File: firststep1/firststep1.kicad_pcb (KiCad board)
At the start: 2 copper layers, 30.5 x 22.9 mm, 12 parts, among them J1 Conn_01x02, J2 Conn_01x03_Male, U1 LM317_TO-220, U2 TL431LP

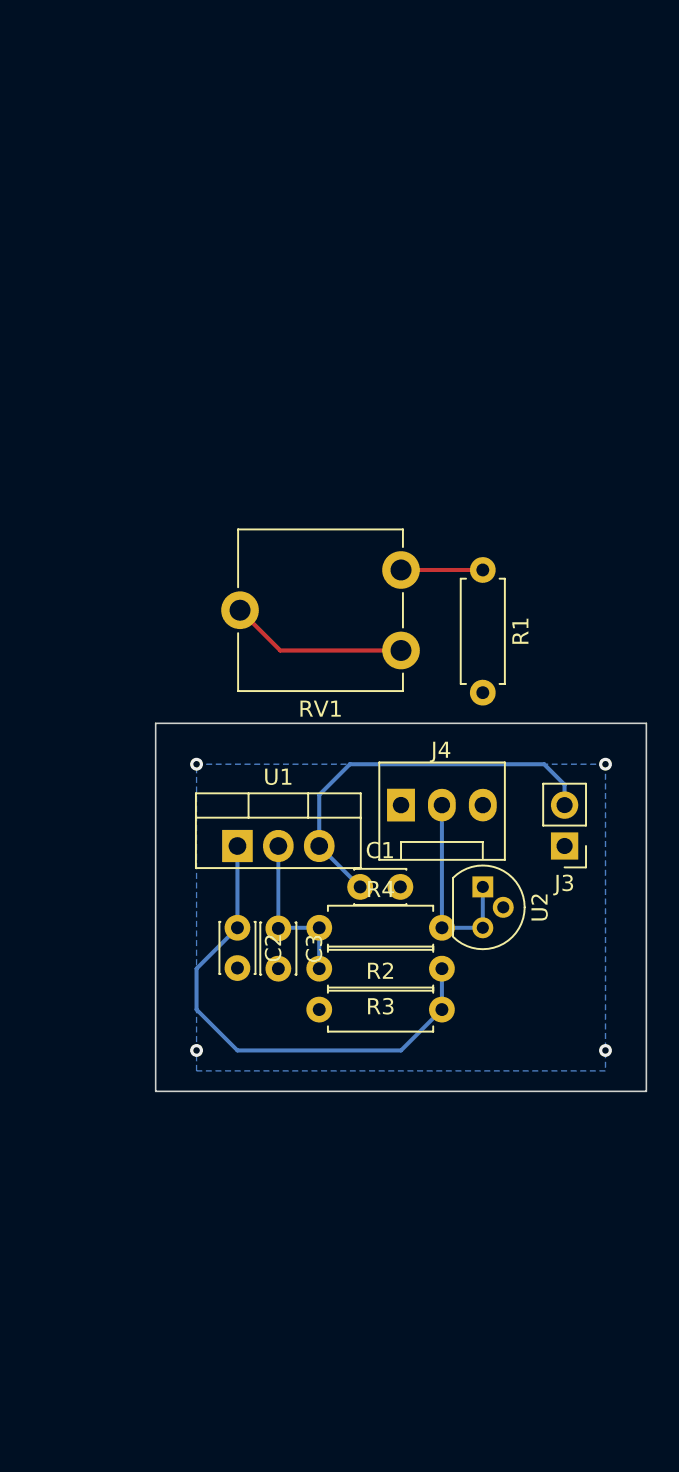
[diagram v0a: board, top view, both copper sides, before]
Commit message: added kicad opeamp
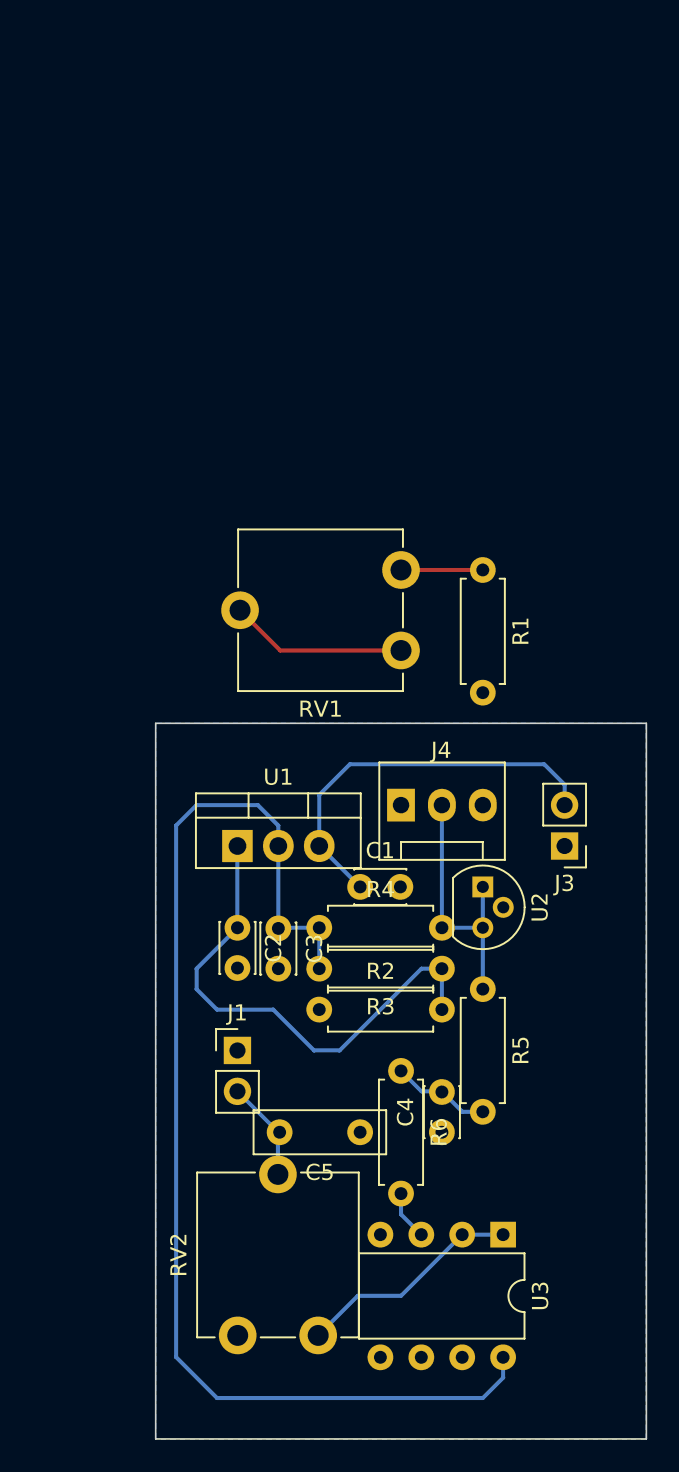
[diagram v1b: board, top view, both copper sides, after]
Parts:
- added C4: 100n, Capacitor_THT:C_Disc_D3.0mm_W2.0mm_P2.50mm, F.Cu at (127.0, 104.1)
- added C5: 4,7u, Capacitor_THT:C_Disc_D8.0mm_W2.5mm_P5.00mm, F.Cu at (121.9, 104.1)
- added J1: Conn_01x02, Connector_PinHeader_2.54mm:PinHeader_1x02_P2.54mm_Vertical, F.Cu at (114.3, 99.1)
- added R2: 330, Resistor_THT:R_Axial_DIN0207_L6.3mm_D2.5mm_P7.62mm_Horizontal, F.Cu at (129.5, 95.2)
- added R2: 330, Resistor_THT:R_Axial_DIN0207_L6.3mm_D2.5mm_P7.62mm_Horizontal, F.Cu at (124.5, 100.3)
- added RV1: R_Potentiometer, Potentiometer_THT:Potentiometer_ACP_CA9-V10_Vertical, F.Cu at (119.3, 116.8)
- added U3: LM358, Package_DIP:DIP-8_W7.62mm, F.Cu at (130.8, 110.5)
- C2: value 1u -> 10n
- C3: value 1u -> 100n
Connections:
- net Net-(J4-Pad2) renamed opamp
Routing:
- net Net-(C3-Pad1): track 10.2 -> 75.0 mm
- net Net-(RV2-Pad1): track 0.00 -> 14.1 mm
- net ADC: track 0.00 -> 6.27 mm
- net Net-(C4-Pad2): track 0.00 -> 6.13 mm
- net opamp: track 12.7 -> 16.5 mm
- net Net-(R6-Pad2): track 0.00 -> 3.07 mm
- net GND: vias 1 -> 0
- net (no net): vias 3 -> 0
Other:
- board size 30.5 x 22.9 mm -> 30.5 x 44.5 mm

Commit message: added suppression diode, changed cap values
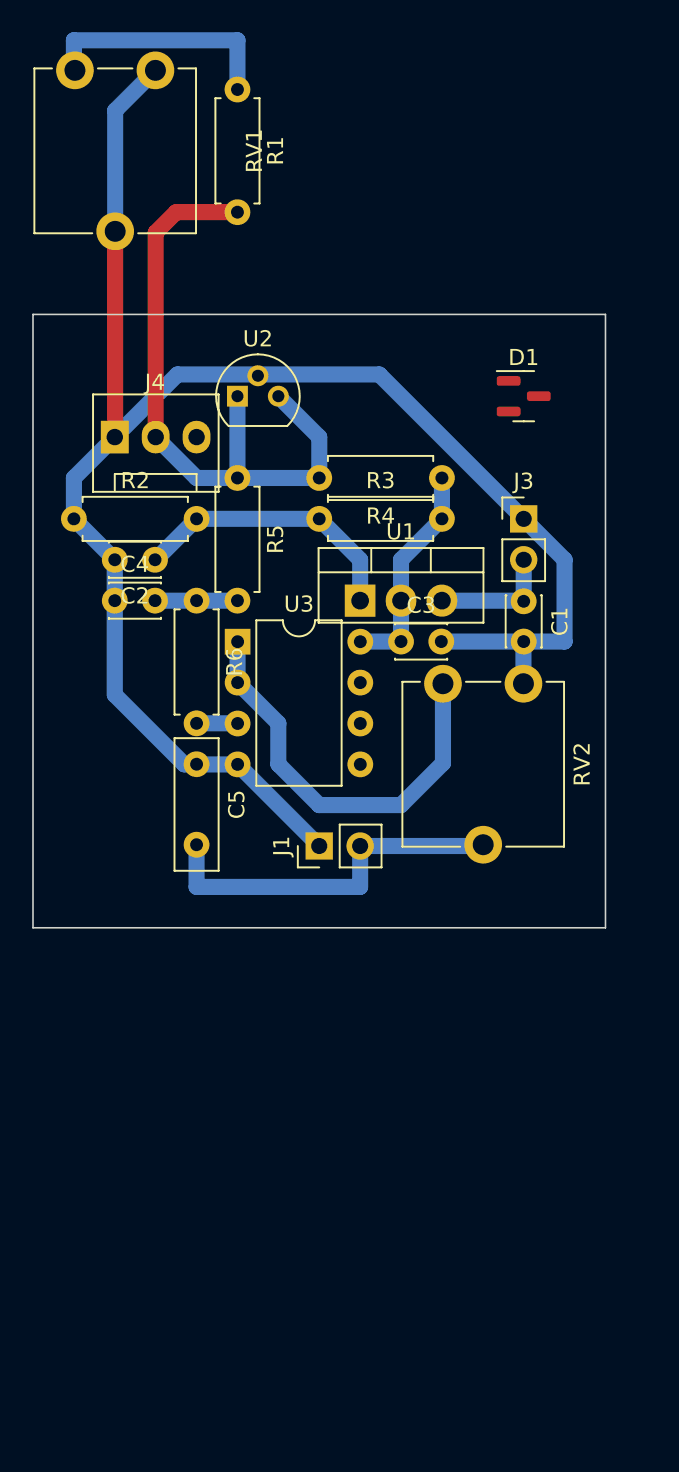
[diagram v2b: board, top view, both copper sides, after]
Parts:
- removed the J1 at (114.3, 99.1)
- removed the J1 at (134.6, 86.4)
- removed the R2 at (129.5, 95.2)
- removed the R2 at (119.4, 96.5)
- removed the R2 at (124.5, 100.3)
- removed the R2 at (127.0, 94.0)
- removed the RV1 at (124.5, 69.2)
- removed the RV1 at (119.3, 116.8)
- added D1: SP0502BAHT, Package_TO_SOT_SMD:SOT-23, F.Cu at (132.1, 58.4)
- added J1: Conn_01x02, Connector_PinHeader_2.54mm:PinHeader_1x02_P2.54mm_Vertical, F.Cu at (119.4, 86.4)
- added J1: Conn_01x02, Connector_PinHeader_2.54mm:PinHeader_1x02_P2.54mm_Vertical, F.Cu at (132.1, 66.0)
- added R2: 470, Resistor_THT:R_Axial_DIN0207_L6.3mm_D2.5mm_P7.62mm_Horizontal, F.Cu at (104.1, 66.0)
- added R2: 330, Resistor_THT:R_Axial_DIN0207_L6.3mm_D2.5mm_P7.62mm_Horizontal, F.Cu at (114.3, 63.5)
- added R2: 330, Resistor_THT:R_Axial_DIN0207_L6.3mm_D2.5mm_P7.62mm_Horizontal, F.Cu at (119.4, 66.0)
- added R2: 330, Resistor_THT:R_Axial_DIN0207_L6.3mm_D2.5mm_P7.62mm_Horizontal, F.Cu at (111.8, 71.1)
- added RV1: R_Potentiometer, Potentiometer_THT:Potentiometer_ACP_CA9-V10_Vertical, F.Cu at (127.1, 76.3)
- added RV1: R_Potentiometer, Potentiometer_THT:Potentiometer_ACP_CA9-V10_Vertical, F.Cu at (104.2, 38.2)
- C2: value 10n -> 0,47u
- C3, C4: value 100n -> 1u
- moved U3 40.4 mm to (114.3, 73.7), turned to 0 degrees
- moved C4 38.8 mm to (106.7, 71.1), turned to 0 degrees
- moved U2 34.1 mm to (114.3, 58.4), turned to 0 degrees
- moved R1 33.5 mm to (114.3, 39.4)
- moved R4 29.0 mm to (127.0, 63.5), turned to 180 degrees
- moved J2 29.0 mm to (106.7, 61.0)
- moved C5 25.0 mm to (111.8, 81.3), turned to -90 degrees
- moved C2 23.4 mm to (109.2, 68.6), turned to 180 degrees
- moved C1 20.4 mm to (132.1, 71.2), turned to -90 degrees
- moved C3 19.4 mm to (124.5, 73.7), turned to 0 degrees
- moved U1 17.0 mm to (121.9, 71.1)
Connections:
- R4 pad 1: Net-(C3-Pad1) -> opamp
- R4 pad 2: opamp -> Net-(C3-Pad1)
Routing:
- net GND: track 11.0 -> 108.3 mm
- net Net-(C3-Pad1): track 75.0 -> 13.7 mm
- net opamp: track 16.5 -> 40.7 mm
- net +5V: track 24.6 -> 7.77 mm
- net ADC: track 6.27 -> 23.0 mm
- net Net-(C2-Pad1): track 31.4 -> 17.4 mm
- net Net-(RV2-Pad1): track 14.1 -> 25.9 mm
- net Net-(R1-Pad1): track 5.08 -> 15.1 mm
- net Net-(C4-Pad2): track 6.13 -> 5.12 mm
- net Net-(R6-Pad2): track 3.07 -> 2.55 mm
- removed copper zone on B.Cu, net GND
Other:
- board size 30.5 x 44.5 mm -> 35.6 x 38.1 mm

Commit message: many changes
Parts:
- C5: value 4,7u -> 0,05; footprint Capacitor_THT:C_Disc_D8.0mm_W2.5mm_P5.00mm -> Capacitor_THT:C_Disc_D3.0mm_W1.6mm_P2.50mm
- moved D1 6.48 mm to (125.7, 59.7)
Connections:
- J1 pad 1: GND -> unconnected-(J1-Pad1)
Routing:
- net opamp: track 40.7 -> 54.3 mm, vias 0 -> 1
- net GND: track 108.3 -> 114.5 mm, vias 0 -> 1
- net Net-(C3-Pad1): track 13.7 -> 19.9 mm
